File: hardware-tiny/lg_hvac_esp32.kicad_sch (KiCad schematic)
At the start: 16 parts, among them J1 JST_XH_S3B-XH-A-1_01x03, J2 Conn_01x19_Female_1_to_19, J3 Conn_01x19_Female_20_to_38, U1 TPS82130, U2 TJA1027

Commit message: fixed bom and updated kicad project to kicad7 #17
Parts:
- C2: LCSC C343058 -> C26404
- U1: footprint TPS82130:CONV_TPS82140SILR -> Package_LGA:Texas_MicroSiP-8-1EP_2.8x3.0mm_P0.65mm_EP1.1x1.9mm_SMD_ThermalVias

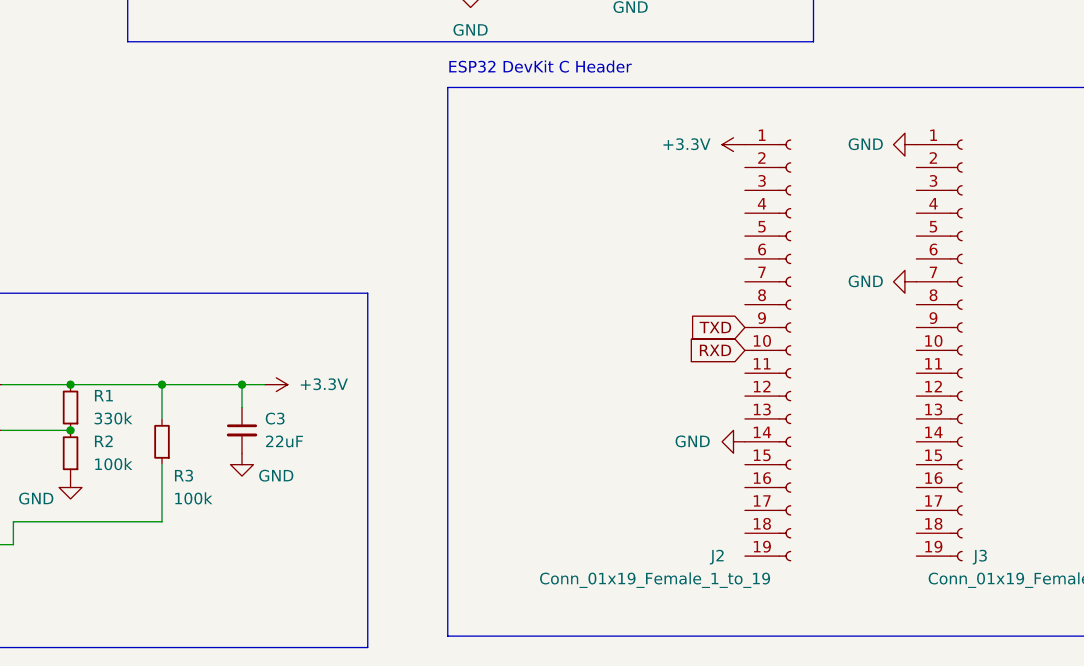
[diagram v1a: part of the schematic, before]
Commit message: fixes in schematic & bom, removed C3
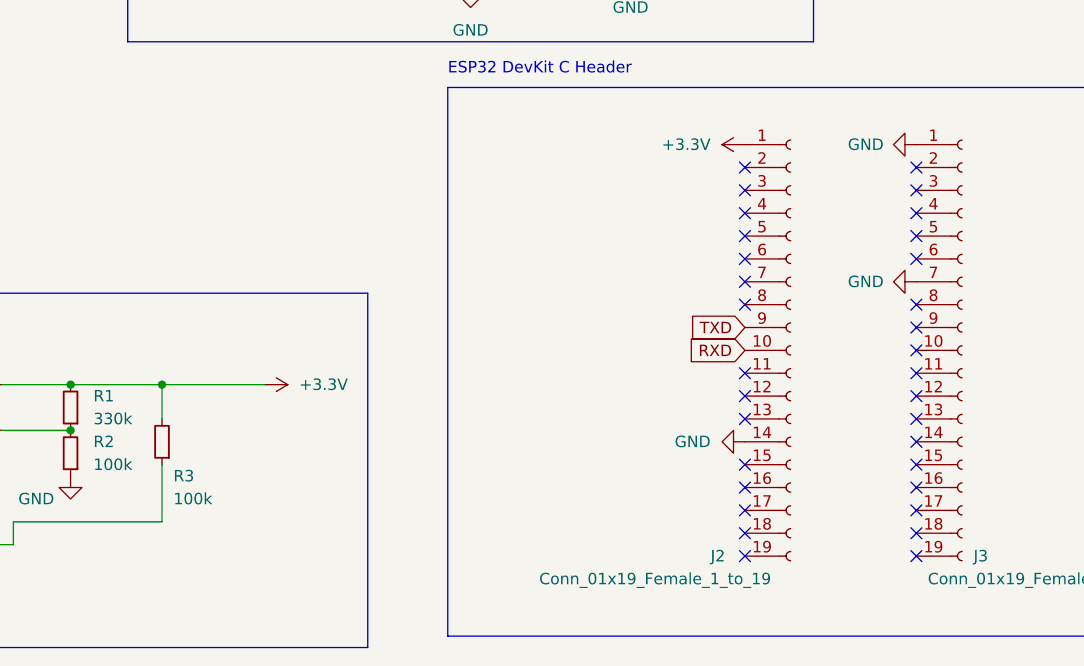
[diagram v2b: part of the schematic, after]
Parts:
- removed C3: 22uF, Capacitor_SMD:CP_Elec_4x5.8, symbol Device:C_Small
- J2, J3: footprint Connector_PinHeader_2.54mm:PinHeader_1x19_P2.54mm_Vertical -> Connector_PinSocket_2.54mm:PinSocket_1x19_P2.54mm_Vertical
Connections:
- no-connect marks 0 -> 32
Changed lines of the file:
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@@
   (junction (at 109.22 26.67) (diameter 0) (color 0 0 0 0)
   )
-  (junction (at 80.01 105.41) (diameter 0) (color 0 0 0 0)
-  )
+  (no_connect (at 135.89 106.68))
+  (no_connect (at 154.94 88.9))
+  (no_connect (at 154.94 99.06))
+  (no_connect (at 135.89 93.98))
+  (no_connect (at 135.89 91.44))
+  (no_connect (at 135.89 119.38))
+  (no_connect (at 135.89 81.28))
+  (no_connect (at 154.94 114.3))
+  (no_connect (at 135.89 88.9))
+  (no_connect (at 135.89 83.82))
+  (no_connect (at 154.94 101.6))
+  (no_connect (at 154.94 121.92))
+  (no_connect (at 154.94 83.82))
+  (no_connect (at 154.94 119.38))
+  (no_connect (at 135.89 124.46))
+  (no_connect (at 154.94 109.22))
+  (no_connect (at 135.89 114.3))
+  (no_connect (at 154.94 86.36))
+  (no_connect (at 154.94 124.46))
+  (no_connect (at 154.94 96.52))
+  (no_connect (at 154.94 91.44))
+  (no_connect (at 135.89 86.36))
+  (no_connect (at 154.94 81.28))
+  (no_connect (at 135.89 121.92))
+  (no_connect (at 154.94 111.76))
+  (no_connect (at 135.89 116.84))
+  (no_connect (at 154.94 116.84))
+  (no_connect (at 154.94 106.68))
+  (no_connect (at 154.94 104.14))
+  (no_connect (at 135.89 109.22))
+  (no_connect (at 135.89 104.14))
+  (no_connect (at 135.89 96.52))
   (wire (pts (xy 53.34 110.49) (xy 60.96 110.49))
     (stroke (width 0) (type default))
@@
     (stroke (width 0) (type default))
   )
-  (wire (pts (xy 80.01 105.41) (xy 82.55 105.41))
-    (stroke (width 0) (type default))
-  )
   (polyline (pts (xy 57.15 60.96) (xy 20.32 60.96))
     (stroke (width 0) (type default))
@@
     (stroke (width 0) (type default))
   )
-  (wire (pts (xy 71.12 105.41) (xy 80.01 105.41))
+  (wire (pts (xy 71.12 105.41) (xy 82.55 105.41))
     (stroke (width 0) (type default))
   )
@@
   )
   (polyline (pts (xy 67.31 67.31) (xy 143.51 67.31))
-    (stroke (width 0) (type default))
-  )
-  (wire (pts (xy 80.01 105.41) (xy 80.01 107.95))
     (stroke (width 0) (type default))
   )
@@
       (effects (font (size 1.27 1.27)) (justify left))
     )
-    (property "Footprint" "Connector_PinHeader_2.54mm:PinHeader_1x19_P2.54mm_Vertical" (at 140.97 101.6 0)
+    (property "Footprint" "Connector_PinSocket_2.54mm:PinSocket_1x19_P2.54mm_Vertical" (at 140.97 101.6 0)
       (effects (font (size 1.27 1.27)) hide)
     )
@@
     )
   )
-  (symbol (lib_id "power:GND") (at 80.01 113.03 0) (unit 1)
-    (in_bom yes) (on_board yes) (dnp no)
-    (property "Reference" "#PWR0109" (at 80.01 119.38 0)
-      (effects (font (size 1.27 1.27)) hide)
-    )
-    (property "Value" "GND" (at 83.82 115.57 0)
-      (effects (font (size 1.27 1.27)))
-    )
-    (property "Footprint" "" (at 80.01 113.03 0)
-      (effects (font (size 1.27 1.27)) hide)
-    )
-    (property "Datasheet" "" (at 80.01 113.03 0)
-      (effects (font (size 1.27 1.27)) hide)
-    )
-    (pin "1")
-    (instances
-      (project "lg_hvac_esp32"
-        (path "/e63e39d7-6ac0-4ffd-8aa3-1841a4541b55"
-          (reference "#PWR0109") (unit 1)
-        )
-      )
-    )
-  )
   (symbol (lib_id "Connector:Conn_01x19_Female") (at 160.02 101.6 0) (unit 1)
     (in_bom yes) (on_board yes) (dnp no)
@@
       (effects (font (size 1.27 1.27)) (justify left))
     )
-    (property "Footprint" "Connector_PinHeader_2.54mm:PinHeader_1x19_P2.54mm_Vertical" (at 160.02 101.6 0)
+    (property "Footprint" "Connector_PinSocket_2.54mm:PinSocket_1x19_P2.54mm_Vertical" (at 160.02 101.6 0)
       (effects (font (size 1.27 1.27)) hide)
     )
@@
         )
       )
-    )
-  )
-  (symbol (lib_id "Device:C_Small") (at 80.01 110.49 0) (unit 1)
-    (in_bom yes) (on_board yes) (dnp no) (fields_autoplaced)
-    (property "Reference" "C3" (at 82.55 109.2262 0)
-      (effects (font (size 1.27 1.27)) (justify left))
-    )
-    (property "Value" "22uF" (at 82.55 111.7662 0)
-      (effects (font (size 1.27 1.27)) (justify left))
-    )
-    (property "Footprint" "Capacitor_SMD:CP_Elec_4x5.8" (at 80.01 110.49 0)
-      (effects (font (size 1.27 1.27)) hide)
-    )
-    (property "Datasheet" "~" (at 80.01 110.49 0)
-      (effects (font (size 1.27 1.27)) hide)
-    )
-    (property "LCSC" "C401758" (at 80.01 110.49 0)
-      (effects (font (size 1.27 1.27)) hide)
-    )
-    (pin "1")
-    (pin "2")
-    (instances
-      (project "lg_hvac_esp32"
-        (path "/e63e39d7-6ac0-4ffd-8aa3-1841a4541b55"
-          (reference "C3") (unit 1)
-        )
-      )
